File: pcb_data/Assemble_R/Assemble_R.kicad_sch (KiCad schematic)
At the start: 93 parts, among them U1 XIAO-nRF52840

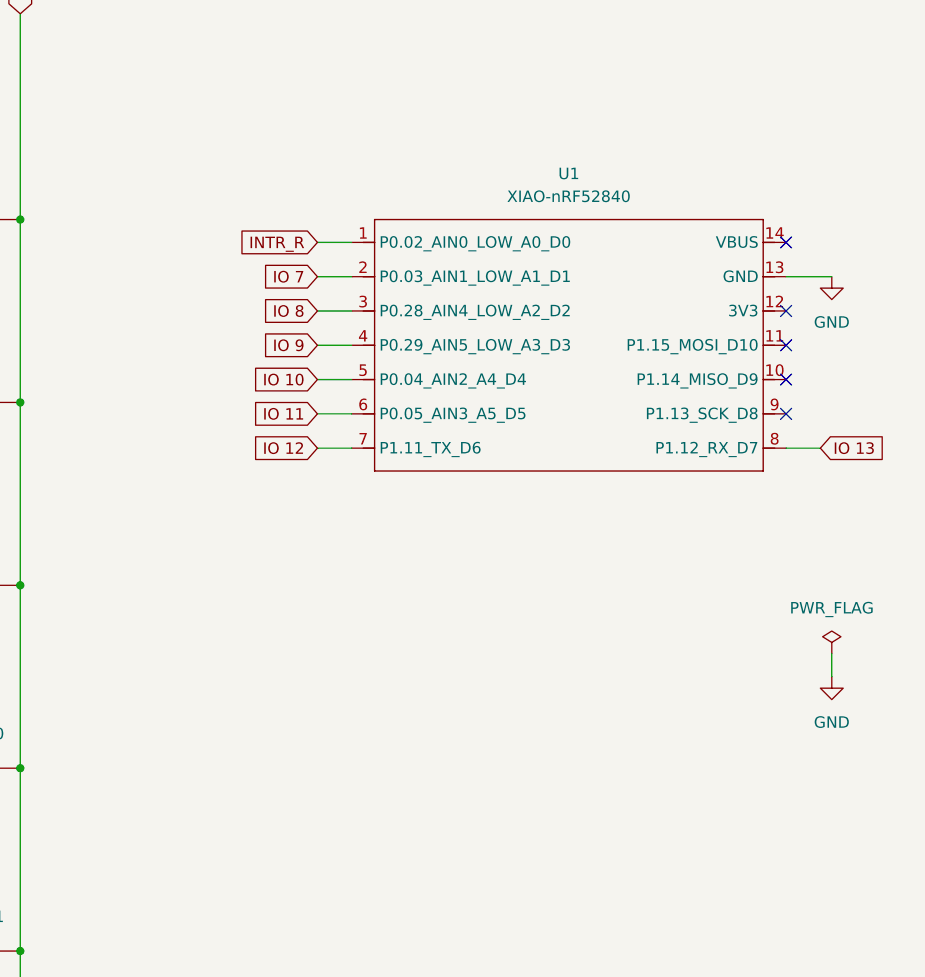
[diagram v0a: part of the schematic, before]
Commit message: replace symbol of xiao-ble
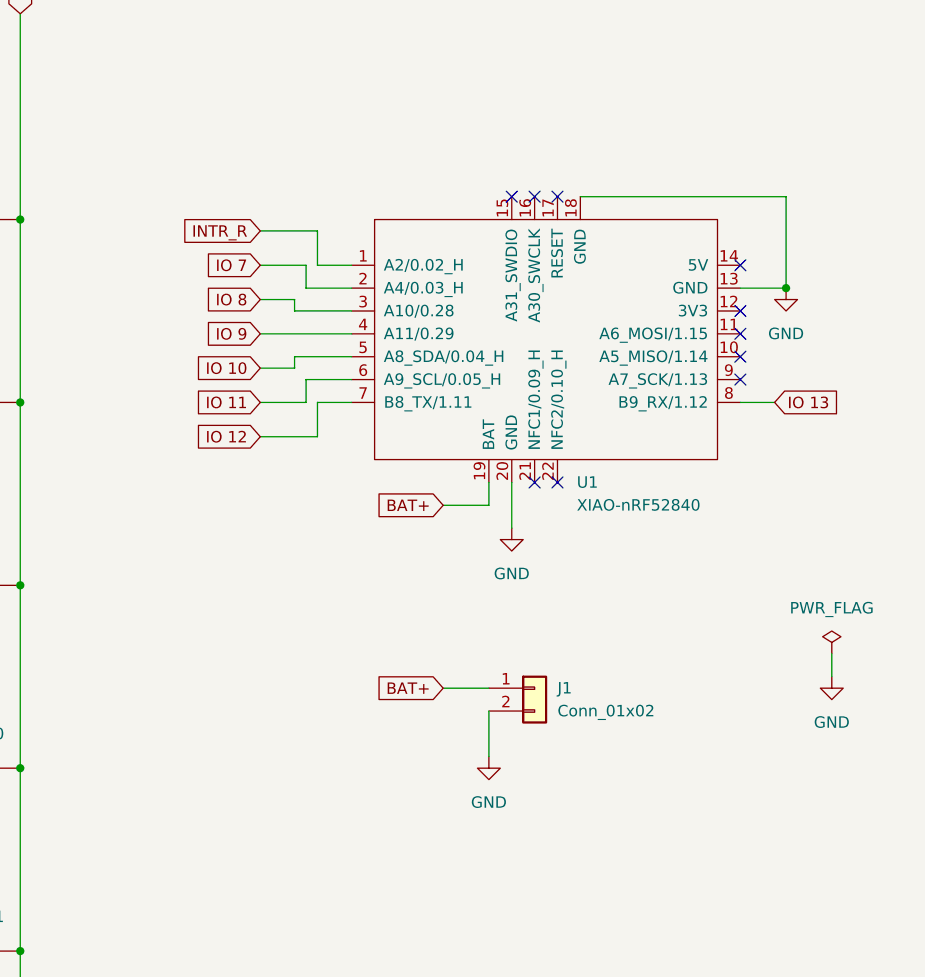
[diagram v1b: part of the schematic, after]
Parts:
- added J1: Conn_01x02, Connector_JST:JST_PH_B2B-PH-K_1x02_P2.00mm_Vertical, symbol Connector_Generic:Conn_01x02
- U1: footprint Seeed Studio XIAO Series Library:XIAO-nRF52840-DIP -> mcu:xiao-ble-smd-cutout; symbol Seeed_Studio_XIAO_Series:XIAO-nRF52840-DIP -> mcu:xiao-ble
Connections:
- net GND: now also U1.18 (GND), U1.20 (GND), J1.2 (Pin_2)
- new net BAT+: J1.1 (Pin_1), U1.19 (BAT)
- no-connect marks 5 -> 10
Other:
- moved on the sheet: U1

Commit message: add component-class field
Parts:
- U1: Component Class (none) -> CastellatedModule
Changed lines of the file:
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@@
+			)
+		)
+		(property "Component Class" "CastellatedModule"
+			(at 234.95 63.5 0)
+			(effects
+				(font
+					(size 1.27 1.27)
+				)
+				(hide yes)
 			)
 		)

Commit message: add mount hole component
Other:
- added sheet MountingHoles (MountingHoles.kicad_sch)
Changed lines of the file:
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@@
+		)
+	)
+	(sheet
+		(at 251.46 152.4)
+		(size 12.7 8.89)
+		(exclude_from_sim no)
+		(in_bom yes)
+		(on_board yes)
+		(dnp no)
+		(fields_autoplaced yes)
+		(stroke
+			(width 0.1524)
+			(type solid)
+		)
+		(fill
+			(color 0 0 0 0.0000)
+		)
+		(property "Sheetname" "MountingHoles"
+			(at 251.46 151.6884 0)
+			(effects
+				(font
+					(size 1.27 1.27)
+				)
+				(justify left bottom)
+			)
+		)
+		(property "Sheetfile" "MountingHoles.kicad_sch"
+			(at 251.46 161.8746 0)
+			(effects
+				(font
+					(size 1.27 1.27)
+				)
+				(justify left top)
+			)
+		)
+		(instances
+			(project "Assemble_R"
+				(path "/38d74f02-042c-4f1b-a14f-ae40b0d0e57e"
+					(page "2")
+				)
+			)
 		)
 	)
